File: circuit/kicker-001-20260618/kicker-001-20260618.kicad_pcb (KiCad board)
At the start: 2 copper layers, 71.4 x 59.3 mm, 56 parts, among them J1 Solenoid_{Stroke}, J2 Solenoid_{Chip}, J3 Drribler_{Front}, J4 Conn_Relay, J6 Voltmeter, Q1 BSS138, Q2 TJ15S06M3L, Q3 Q_Photo_CE, Q4 MTB010N06RJ3, Q5 MTB010N06RJ3, U1 NOT, U10 TLP2361, U11 AND, U12 AND, U2 TLP2361, U3 XL6009E1, U4 NOT, U5 NOT, U6 DRV8874, U7 NOT, U8 NOT, U9 TLP2361

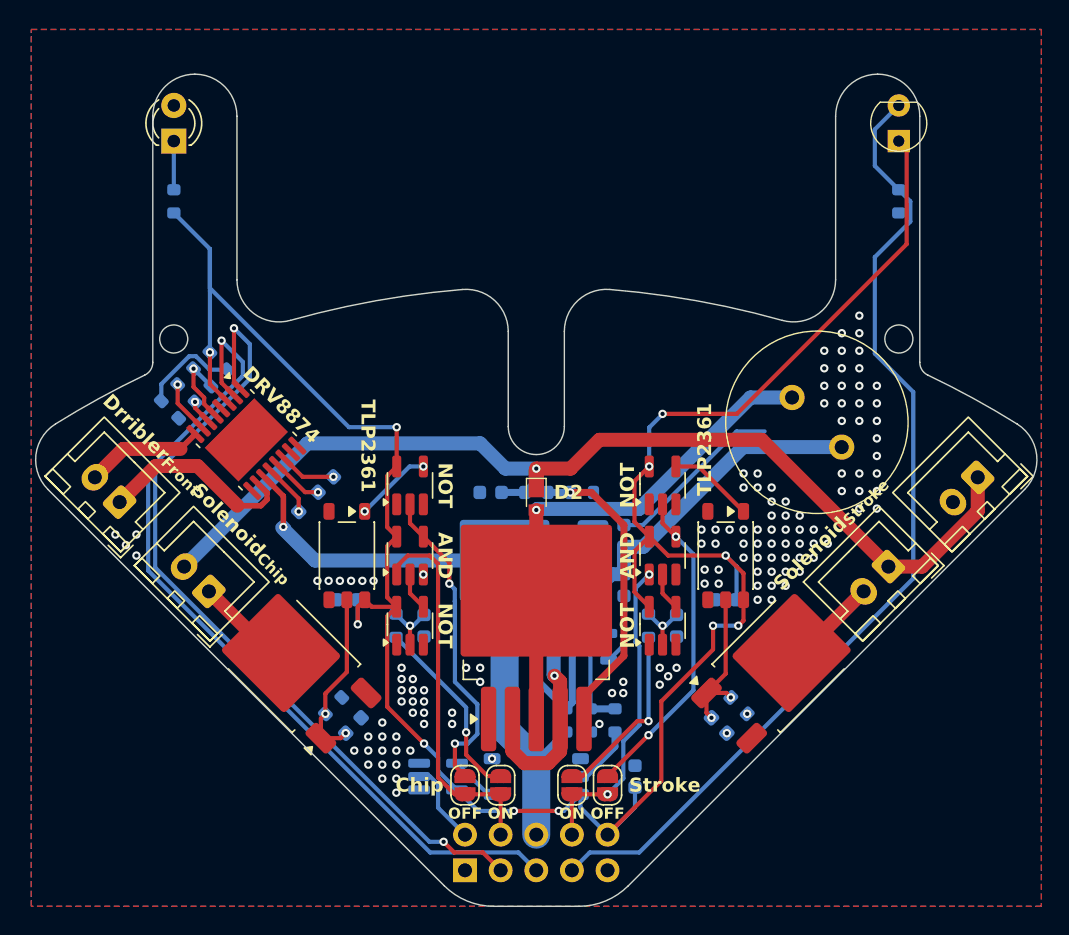
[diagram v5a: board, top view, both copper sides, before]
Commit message: Update キッカー基板のボード図完成させた、DRは一日おいてから
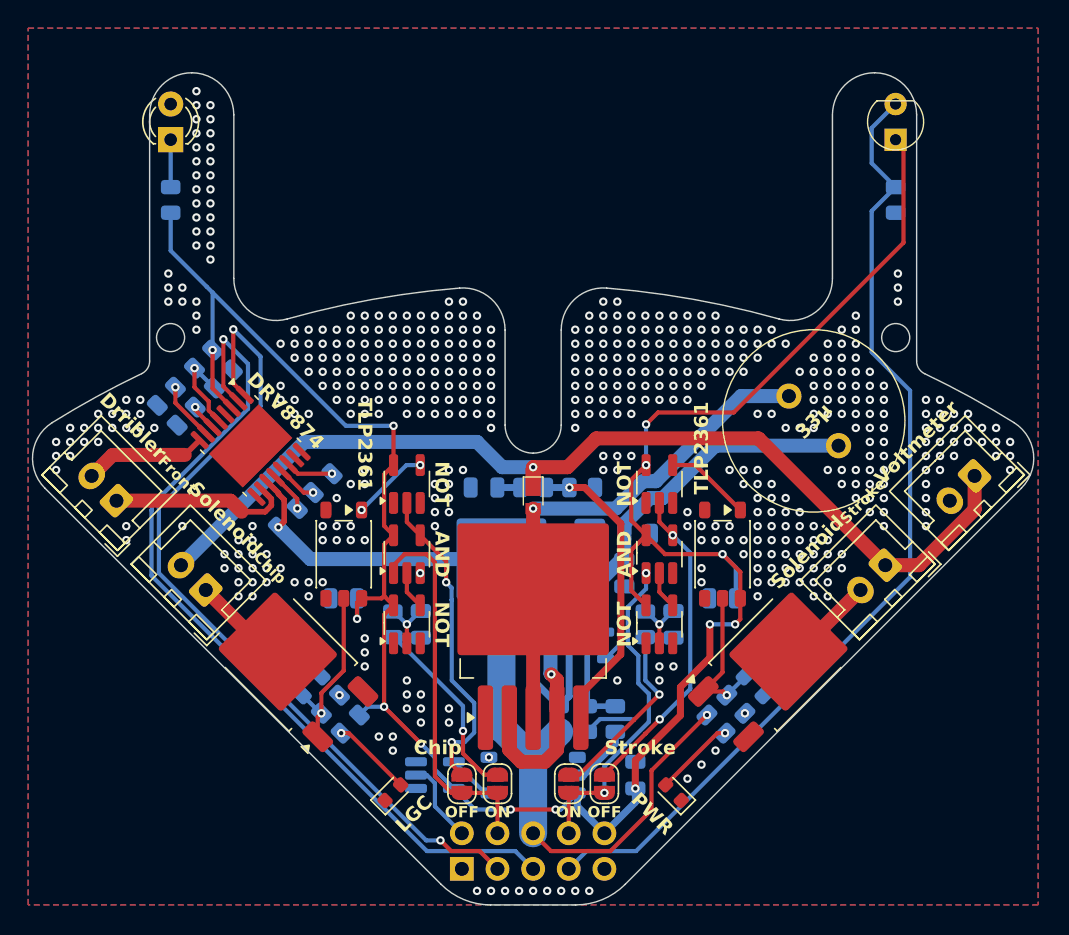
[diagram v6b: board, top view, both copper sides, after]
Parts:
- added D3: PWR, LED_SMD:LED_0603_1608Metric, F.Cu at (110.0, 92.0)
- added D4: LGC, LED_SMD:LED_0603_1608Metric, F.Cu at (90.0, 92.0)
- added R15: 2.49k, Resistor_SMD:R_0805_2012Metric, B.Cu at (113.0, 87.1)
- added R16: 330, Resistor_SMD:R_0805_2012Metric, B.Cu at (87.0, 87.1)
- C1, C10, C11, C12, C2, C3, C4, C5, C6, C7, C8, C9: footprint Capacitor_SMD:C_0603_1608Metric -> Capacitor_SMD:C_0805_2012Metric
- D2: value D2 -> CUHS20F60
- L1: value 33u -> 33μ
- R1, R10, R11, R12, R13, R14, R17, R2, R3, R4, R5, R6, R7, R8, R9: footprint Resistor_SMD:R_0603_1608Metric -> Resistor_SMD:R_0805_2012Metric
- moved C4 4.23 mm to (84.1, 84.3)
- moved C3 3.92 mm to (115.9, 84.3)
- moved C1 0.99 mm to (107.5, 73.5), turned to 0 degrees
- moved C2 0.85 mm to (106.5, 76.3)
- moved C6 0.59 mm to (96.5, 70.2)
- moved U6 0.53 mm to (79.9, 67.3)
- moved R3 0.49 mm to (101.9, 86.7)
- moved R10 0.43 mm to (75.3, 65.2)
- moved R9 0.42 mm to (100.0, 70.2)
- moved R7 0.35 mm to (103.5, 70.2)
- moved R17 0.34 mm to (73.9, 63.7)
- moved R14 0.31 mm to (77.9, 62.5)
- moved U8 0.25 mm to (91.0, 80.0)
- moved JP2 0.25 mm to (105.1, 91.4)
- moved R4 0.25 mm to (125.8, 49.7)
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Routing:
- net GND: track 24.9 -> 8.54 mm, vias 131 -> 497
- net VCC: track 49.5 -> 63.1 mm, vias 1 -> 2
- net +3.3V: track 169.4 -> 163.2 mm, vias 11 -> 13
- net Net-(D4-A): track 0.00 -> 5.76 mm, vias 0 -> 1
- net Net-(D3-A): track 0.00 -> 5.76 mm, vias 0 -> 1
- net OUT2_{Dribbler-Front}: track 14.3 -> 12.9 mm
- net Kick_{Stroke}: track 22.5 -> 23.6 mm
- net VREF_{Dribbler-Front}: track 5.66 -> 6.56 mm
- net BallCatch_{Front}: track 70.6 -> 69.9 mm
- net EN_{Dribbler-Front}: track 58.4 -> 59.1 mm
- net PH_{Dribbler-Front}: track 60.6 -> 61.2 mm
- net ^{SAFE}Kick_{Chip}: vias 2 -> 1
- net ^{SAFE}Kick_{Stroke}: vias 2 -> 1
